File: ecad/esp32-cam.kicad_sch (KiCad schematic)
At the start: 1 part, among them U1 ESP32-CAM

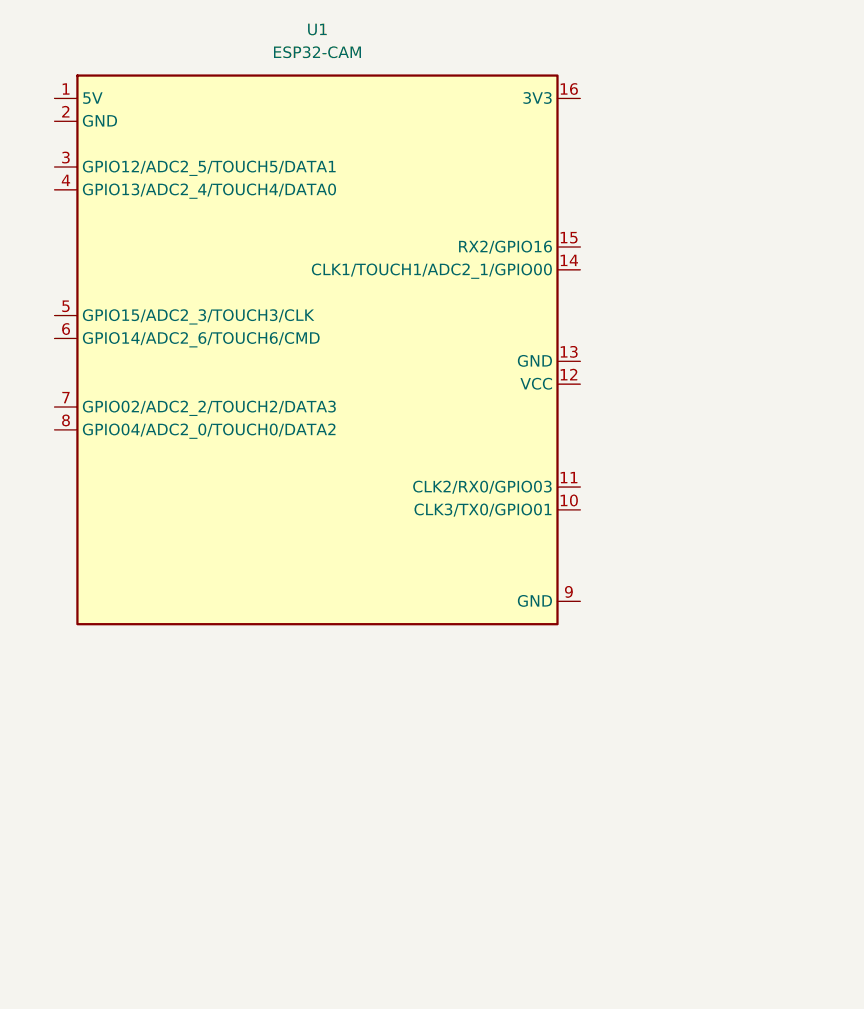
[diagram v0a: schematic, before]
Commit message: fead (ecad): update ESP32-CAM Schematic
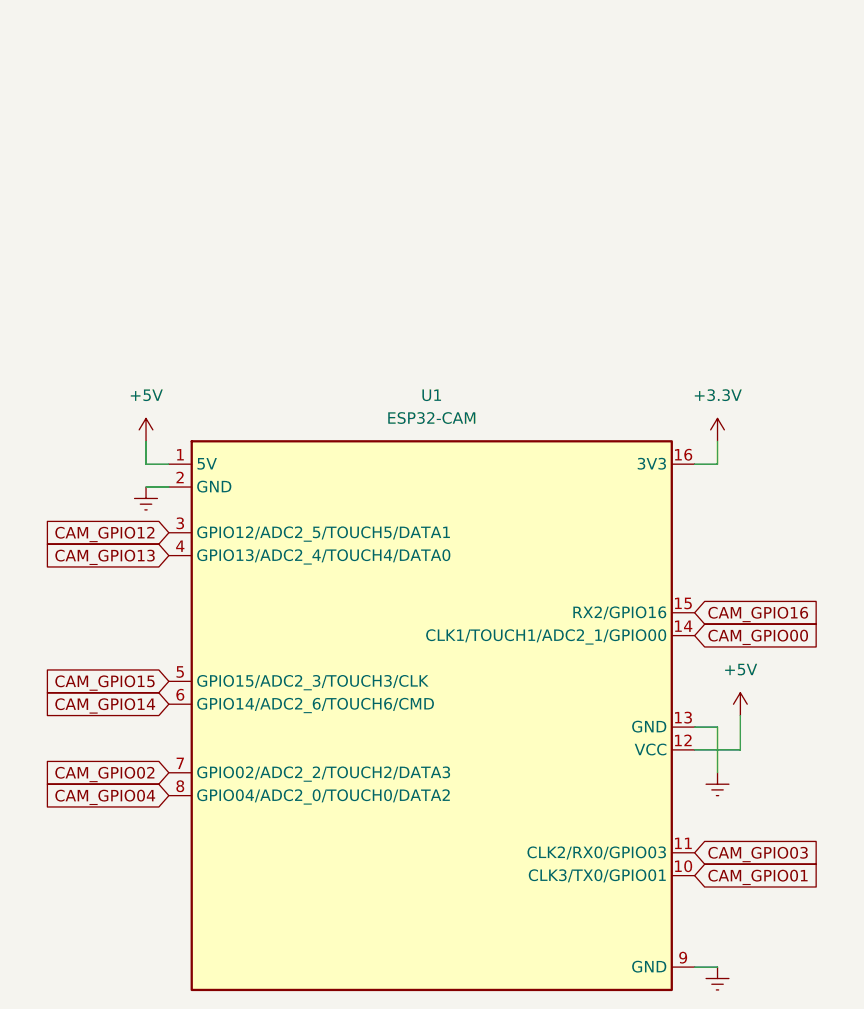
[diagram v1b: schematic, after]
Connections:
- net +5V: now reaches U1.1 (5V)
- net +5V: now also U1.12 (VCC)
- net CAM_GPIO01: now reaches U1.10 (CLK3/TX0/GPIO01)
- net CAM_GPIO03: now reaches U1.11 (CLK2/RX0/GPIO03)
- net Earth: now reaches U1.13 (GND)
- net Earth: now also U1.2 (GND), U1.9 (GND)
- net CAM_GPIO00: now reaches U1.14 (CLK1/TOUCH1/ADC2_1/GPIO00)
- net CAM_GPIO16: now reaches U1.15 (RX2/GPIO16)
- net +3.3V: now reaches U1.16 (3V3)
- net CAM_GPIO12: now reaches U1.3 (GPIO12/ADC2_5/TOUCH5/DATA1)
- net CAM_GPIO13: now reaches U1.4 (GPIO13/ADC2_4/TOUCH4/DATA0)
- net CAM_GPIO15: now reaches U1.5 (GPIO15/ADC2_3/TOUCH3/CLK)
- net CAM_GPIO14: now reaches U1.6 (GPIO14/ADC2_6/TOUCH6/CMD)
- net CAM_GPIO02: now reaches U1.7 (GPIO02/ADC2_2/TOUCH2/DATA3)
- net CAM_GPIO04: now reaches U1.8 (GPIO04/ADC2_0/TOUCH0/DATA2)
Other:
- title: (none) -> ESP32 AK Shield Schematik drawing CAM
- moved on the sheet: U1
